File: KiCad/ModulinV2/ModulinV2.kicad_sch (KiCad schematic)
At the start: 0 parts

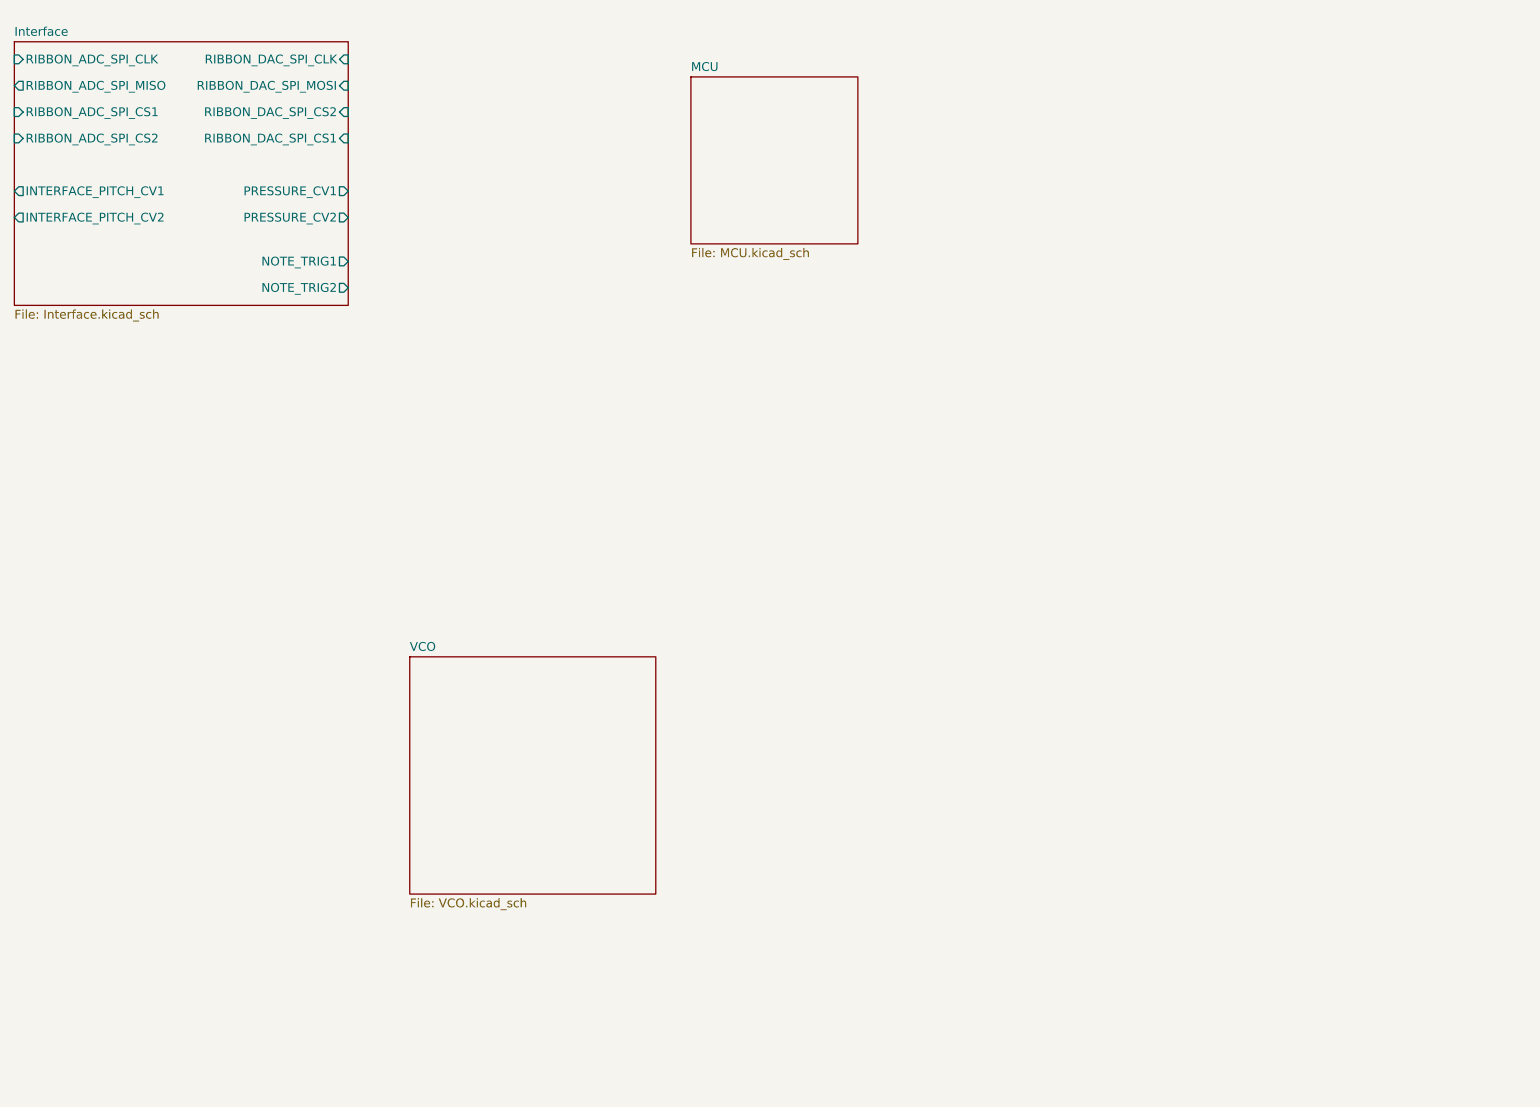
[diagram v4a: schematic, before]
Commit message: Finished 1.0 of the VCO and started making the waveform select module
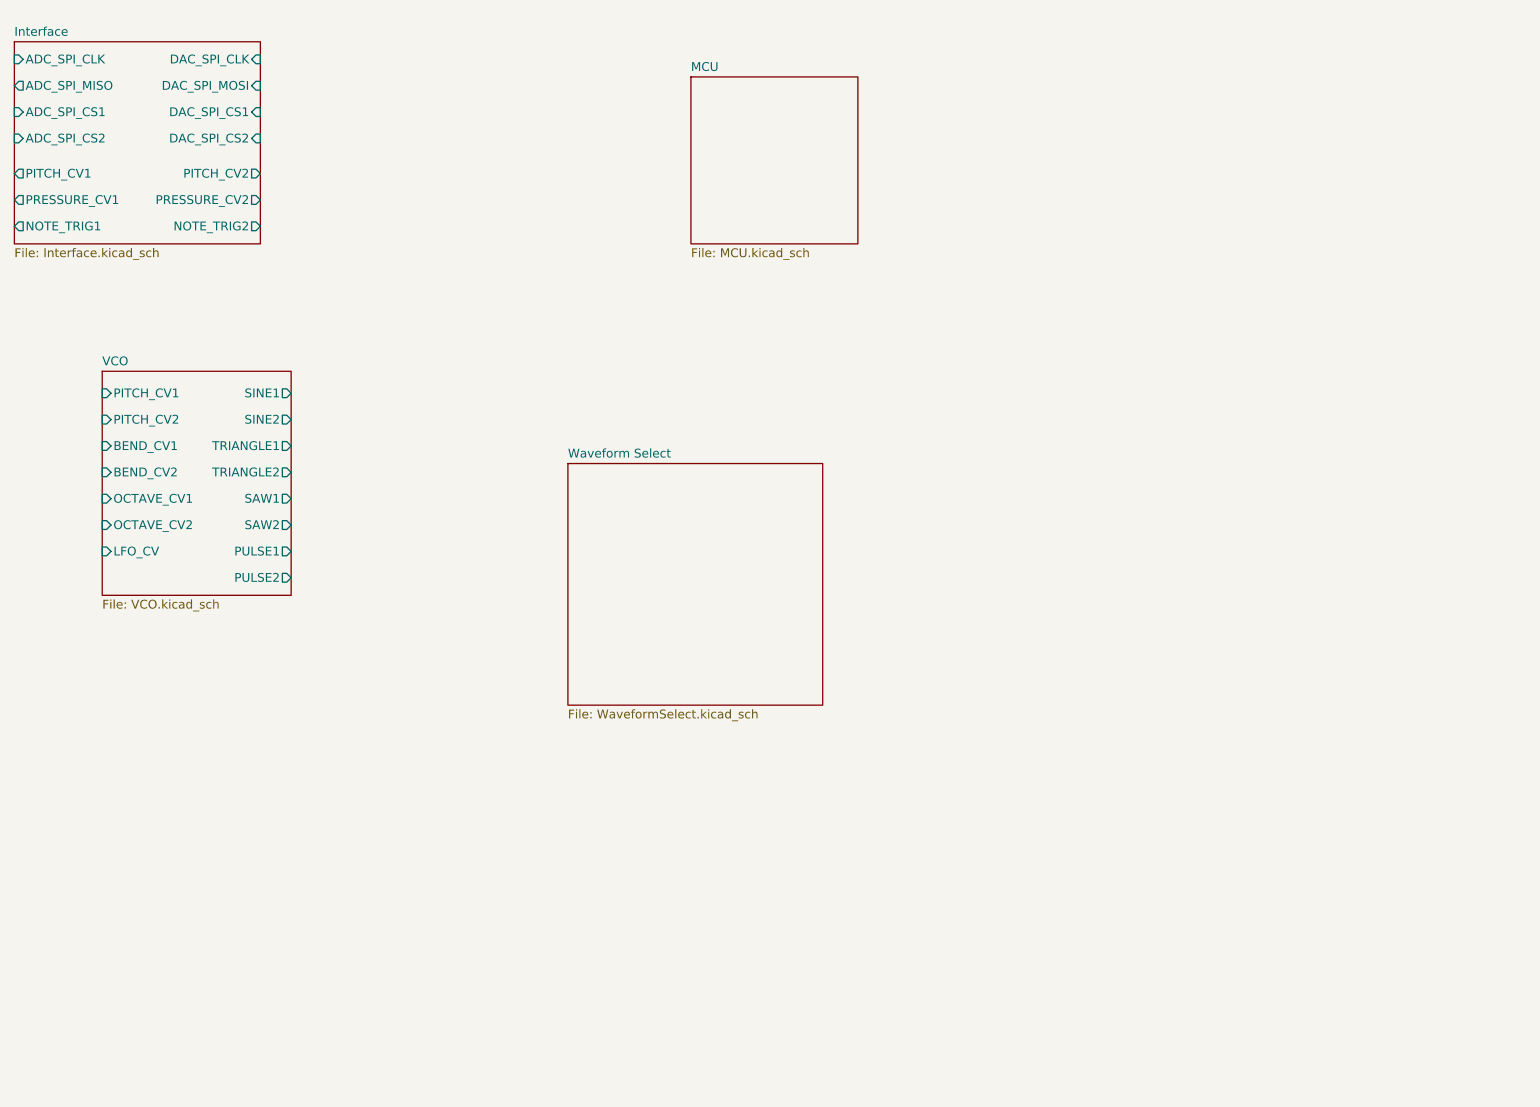
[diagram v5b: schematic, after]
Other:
- added sheet Waveform Select (WaveformSelect.kicad_sch)
- sheet Interface ports: added ADC_SPI_CLK, ADC_SPI_CS1, ADC_SPI_CS2, ADC_SPI_MISO, DAC_SPI_CLK, DAC_SPI_CS1, DAC_SPI_CS2, DAC_SPI_MOSI, PITCH_CV1, PITCH_CV2; removed INTERFACE_PITCH_CV1, INTERFACE_PITCH_CV2, RIBBON_ADC_SPI_CLK, RIBBON_ADC_SPI_CS1, RIBBON_ADC_SPI_CS2, RIBBON_ADC_SPI_MISO, RIBBON_DAC_SPI_CLK, RIBBON_DAC_SPI_CS1, RIBBON_DAC_SPI_CS2, RIBBON_DAC_SPI_MOSI
- sheet VCO ports: added BEND_CV1, BEND_CV2, LFO_CV, OCTAVE_CV1, OCTAVE_CV2, PITCH_CV1, PITCH_CV2, PULSE1, PULSE2, SAW1, SAW2, SINE1, SINE2, TRIANGLE1, TRIANGLE2; removed none
- company: Rasmus Palk -> (none)
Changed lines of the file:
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@@
 	(title_block
 		(title "Modulin V2")
-		(date "2025-04-25")
-		(company "Rasmus Palk")
+		(date "2025-07-13")
+		(rev "1.3")
+		(comment 1 "Instructor: Kaiser Pärnamets")
+		(comment 2 "By: Rasmus Palk")
 	)
 	(sheet
 		(at 21.59 29.21)
-		(size 48.26 38.1)
+		(size 35.56 29.21)
 		(exclude_from_sim no)
 		(in_bom yes)
@@
 		)
 		(property "Sheetfile" "Interface.kicad_sch"
-			(at 21.59 67.8946 0)
+			(at 21.59 59.0046 0)
 			(effects
 				(font
@@
 		)
 		(pin "PRESSURE_CV1" output
-			(at 69.85 50.8 0)
-			(effects
-				(font
-					(size 1.27 1.27)
-				)
-				(justify right)
-			)
-		)
-		(pin "INTERFACE_PITCH_CV2" output
-			(at 21.59 54.61 180)
+			(at 21.59 52.07 180)
 			(effects
 				(font
@@
 		)
 		(pin "PRESSURE_CV2" output
-			(at 69.85 54.61 0)
+			(at 57.15 52.07 0)
 			(effects
 				(font
@@
 		)
 		(pin "NOTE_TRIG2" output
-			(at 69.85 64.77 0)
+			(at 57.15 55.88 0)
 			(effects
 				(font
@@
 		)
 		(pin "NOTE_TRIG1" output
-			(at 69.85 60.96 0)
-			(effects
-				(font
-					(size 1.27 1.27)
-				)
-				(justify right)
-			)
-		)
-		(pin "INTERFACE_PITCH_CV1" output
-			(at 21.59 50.8 180)
-			(effects
-				(font
-					(size 1.27 1.27)
-				)
-				(justify left)
-			)
-		)
-		(pin "RIBBON_ADC_SPI_CLK" input
+			(at 21.59 55.88 180)
+			(effects
+				(font
+					(size 1.27 1.27)
+				)
+				(justify left)
+			)
+		)
+		(pin "DAC_SPI_MOSI" input
+			(at 57.15 35.56 0)
+			(effects
+				(font
+					(size 1.27 1.27)
+				)
+				(justify right)
+			)
+		)
+		(pin "PITCH_CV1" output
+			(at 21.59 48.26 180)
+			(effects
+				(font
+					(size 1.27 1.27)
+				)
+				(justify left)
+			)
+		)
+		(pin "DAC_SPI_CS1" input
+			(at 57.15 39.37 0)
+			(effects
+				(font
+					(size 1.27 1.27)
+				)
+				(justify right)
+			)
+		)
+		(pin "ADC_SPI_MISO" output
+			(at 21.59 35.56 180)
+			(effects
+				(font
+					(size 1.27 1.27)
+				)
+				(justify left)
+			)
+		)
+		(pin "ADC_SPI_CLK" input
 			(at 21.59 31.75 180)
 			(effects
@@
 			)
 		)
-		(pin "RIBBON_DAC_SPI_CLK" input
-			(at 69.85 31.75 0)
-			(effects
-				(font
-					(size 1.27 1.27)
-				)
-				(justify right)
-			)
-		)
-		(pin "RIBBON_ADC_SPI_CS1" input
+		(pin "PITCH_CV2" output
+			(at 57.15 48.26 0)
+			(effects
+				(font
+					(size 1.27 1.27)
+				)
+				(justify right)
+			)
+		)
+		(pin "DAC_SPI_CLK" input
+			(at 57.15 31.75 0)
+			(effects
+				(font
+					(size 1.27 1.27)
+				)
+				(justify right)
+			)
+		)
+		(pin "ADC_SPI_CS2" input
+			(at 21.59 43.18 180)
+			(effects
+				(font
+					(size 1.27 1.27)
+				)
+				(justify left)
+			)
+		)
+		(pin "ADC_SPI_CS1" input
 			(at 21.59 39.37 180)
 			(effects
@@
 			)
 		)
-		(pin "RIBBON_DAC_SPI_CS1" input
-			(at 69.85 43.18 0)
-			(effects
-				(font
-					(size 1.27 1.27)
-				)
-				(justify right)
-			)
-		)
-		(pin "RIBBON_DAC_SPI_MOSI" input
-			(at 69.85 35.56 0)
-			(effects
-				(font
-					(size 1.27 1.27)
-				)
-				(justify right)
-			)
-		)
-		(pin "RIBBON_DAC_SPI_CS2" input
-			(at 69.85 39.37 0)
-			(effects
-				(font
-					(size 1.27 1.27)
-				)
-				(justify right)
-			)
-		)
-		(pin "RIBBON_ADC_SPI_MISO" output
-			(at 21.59 35.56 180)
-			(effects
-				(font
-					(size 1.27 1.27)
-				)
-				(justify left)
-			)
-		)
-		(pin "RIBBON_ADC_SPI_CS2" input
-			(at 21.59 43.18 180)
-			(effects
-				(font
-					(size 1.27 1.27)
-				)
-				(justify left)
+		(pin "DAC_SPI_CS2" input
+			(at 57.15 43.18 0)
+			(effects
+				(font
+					(size 1.27 1.27)
+				)
+				(justify right)
 			)
 		)
@@
 	)
 	(sheet
-		(at 78.74 118.11)
-		(size 35.56 34.29)
+		(at 34.29 76.835)
+		(size 27.305 32.385)
 		(exclude_from_sim no)
 		(in_bom yes)
@@
 		)
 		(property "Sheetname" "VCO"
-			(at 78.74 117.3984 0)
+			(at 34.29 76.1234 0)
 			(effects
 				(font
@@
 		)
 		(property "Sheetfile" "VCO.kicad_sch"
-			(at 78.74 152.9846 0)
+			(at 34.29 109.8046 0)
 			(effects
 				(font
@@
 				)
 				(justify left top)
+			)
+		)
+		(pin "LFO_CV" input
+			(at 34.29 102.87 180)
+			(effects
+				(font
+					(size 1.27 1.27)
+				)
+				(justify left)
+			)
+		)
+		(pin "PULSE1" output
+			(at 61.595 102.87 0)
+			(effects
+				(font
+					(size 1.27 1.27)
+				)
+				(justify right)
+			)
+		)
+		(pin "PULSE2" output
+			(at 61.595 106.68 0)
+			(effects
+				(font
+					(size 1.27 1.27)
+				)
+				(justify right)
+			)
+		)
+		(pin "TRIANGLE2" output
+			(at 61.595 91.44 0)
+			(effects
+				(font
+					(size 1.27 1.27)
+				)
+				(justify right)
+			)
+		)
+		(pin "SAW2" output
+			(at 61.595 99.06 0)
+			(effects
+				(font
+					(size 1.27 1.27)
+				)
+				(justify right)
+			)
+		)
+		(pin "SINE2" output
+			(at 61.595 83.82 0)
+			(effects
+				(font
+					(size 1.27 1.27)
+				)
+				(justify right)
+			)
+		)
+		(pin "SAW1" output
+			(at 61.595 95.25 0)
+			(effects
+				(font
+					(size 1.27 1.27)
+				)
+				(justify right)
+			)
+		)
+		(pin "SINE1" output
+			(at 61.595 80.01 0)
+			(effects
+				(font
+					(size 1.27 1.27)
+				)
+				(justify right)
+			)
+		)
+		(pin "TRIANGLE1" output
+			(at 61.595 87.63 0)
+			(effects
+				(font
+					(size 1.27 1.27)
+				)
+				(justify right)
+			)
+		)
+		(pin "PITCH_CV1" input
+			(at 34.29 80.01 180)
+			(effects
+				(font
+					(size 1.27 1.27)
+				)
+				(justify left)
+			)
+		)
+		(pin "PITCH_CV2" input
+			(at 34.29 83.82 180)
+			(effects
+				(font
+					(size 1.27 1.27)
+				)
+				(justify left)
+			)
+		)
+		(pin "BEND_CV2" input
+			(at 34.29 91.44 180)
+			(effects
+				(font
+					(size 1.27 1.27)
+				)
+				(justify left)
+			)
+		)
+		(pin "OCTAVE_CV2" input
+			(at 34.29 99.06 180)
+			(effects
+				(font
+					(size 1.27 1.27)
+				)
+				(justify left)
+			)
+		)
+		(pin "OCTAVE_CV1" input
+			(at 34.29 95.25 180)
+			(effects
+				(font
+					(size 1.27 1.27)
+				)
+				(justify left)
+			)
+		)
+		(pin "BEND_CV1" input
+			(at 34.29 87.63 180)
+			(effects
+				(font
+					(size 1.27 1.27)
+				)
+				(justify left)
 			)
 		)
@@
 				)
 			)
+		)
+	)
+	(sheet
+		(at 101.6 90.17)
+		(size 36.83 34.925)
+		(exclude_from_sim no)
+		(in_bom yes)
+		(on_board yes)
+		(dnp no)
+		(fields_autoplaced yes)
+		(stroke
+			(width 0.1524)
+			(type solid)
+		)
+		(fill
+			(color 0 0 0 0.0000)
+		)
+		(property "Sheetname" "Waveform Select"
+			(at 101.6 89.4584 0)
+			(effects
+				(font
+					(size 1.27 1.27)
+				)
+				(justify left bottom)
+			)
+		)
+		(property "Sheetfile" "WaveformSelect.kicad_sch"
+			(at 101.6 125.6796 0)
+			(effects
+				(font
+					(size 1.27 1.27)
+				)
+				(justify left top)
+			)
+		)
+		(instances
+			(project "ModulinV2"
+				(path "/c6b34a57-3941-4b56-8b80-1848c7f41082"
+					(page "5")
+				)
+			)

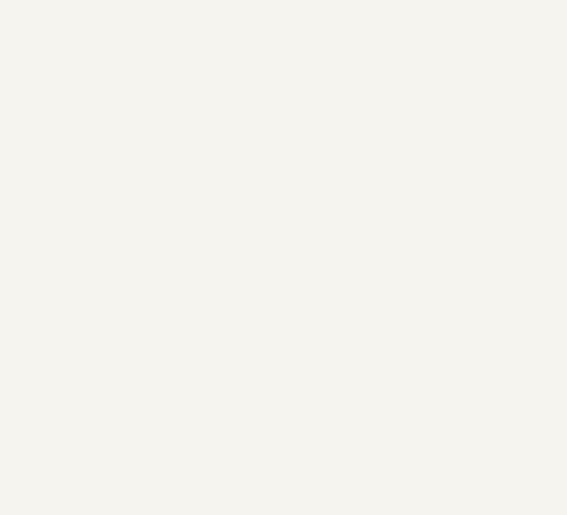
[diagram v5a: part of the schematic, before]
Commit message: Made initial AS3360 VCA schematic
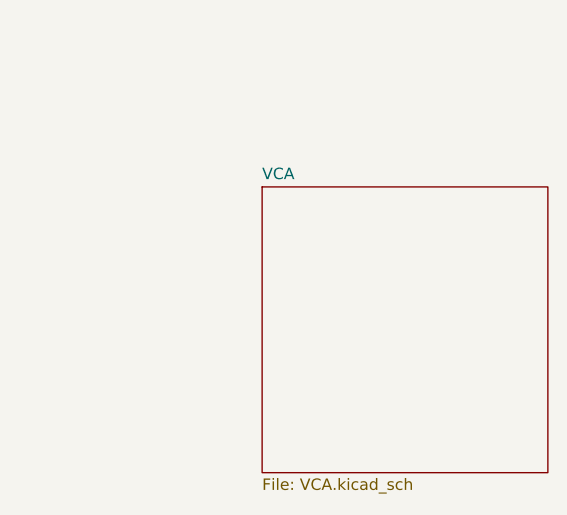
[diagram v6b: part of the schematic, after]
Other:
- added sheet VCA (VCA.kicad_sch)
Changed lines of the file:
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@@
+	)
+	(sheet
+		(at 172.72 99.06)
+		(size 31.75 31.75)
+		(exclude_from_sim no)
+		(in_bom yes)
+		(on_board yes)
+		(dnp no)
+		(fields_autoplaced yes)
+		(stroke
+			(width 0.1524)
+			(type solid)
+		)
+		(fill
+			(color 0 0 0 0.0000)
+		)
+		(property "Sheetname" "VCA"
+			(at 172.72 98.3484 0)
+			(effects
+				(font
+					(size 1.27 1.27)
+				)
+				(justify left bottom)
+			)
+		)
+		(property "Sheetfile" "VCA.kicad_sch"
+			(at 172.72 131.3946 0)
+			(effects
+				(font
+					(size 1.27 1.27)
+				)
+				(justify left top)
+			)
+		)
+		(instances
+			(project "ModulinV2"
+				(path "/c6b34a57-3941-4b56-8b80-1848c7f41082"
+					(page "6")
+				)
+			)
+		)
 	)
 	(sheet
